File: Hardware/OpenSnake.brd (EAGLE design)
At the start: 25.4 x 25.4 mm, 36 parts, among them J1 microB, Q1 16MHZ, U1 ATMEGA328P_TQFP, U3 CH340G, U4 5V, Y2 12MHz

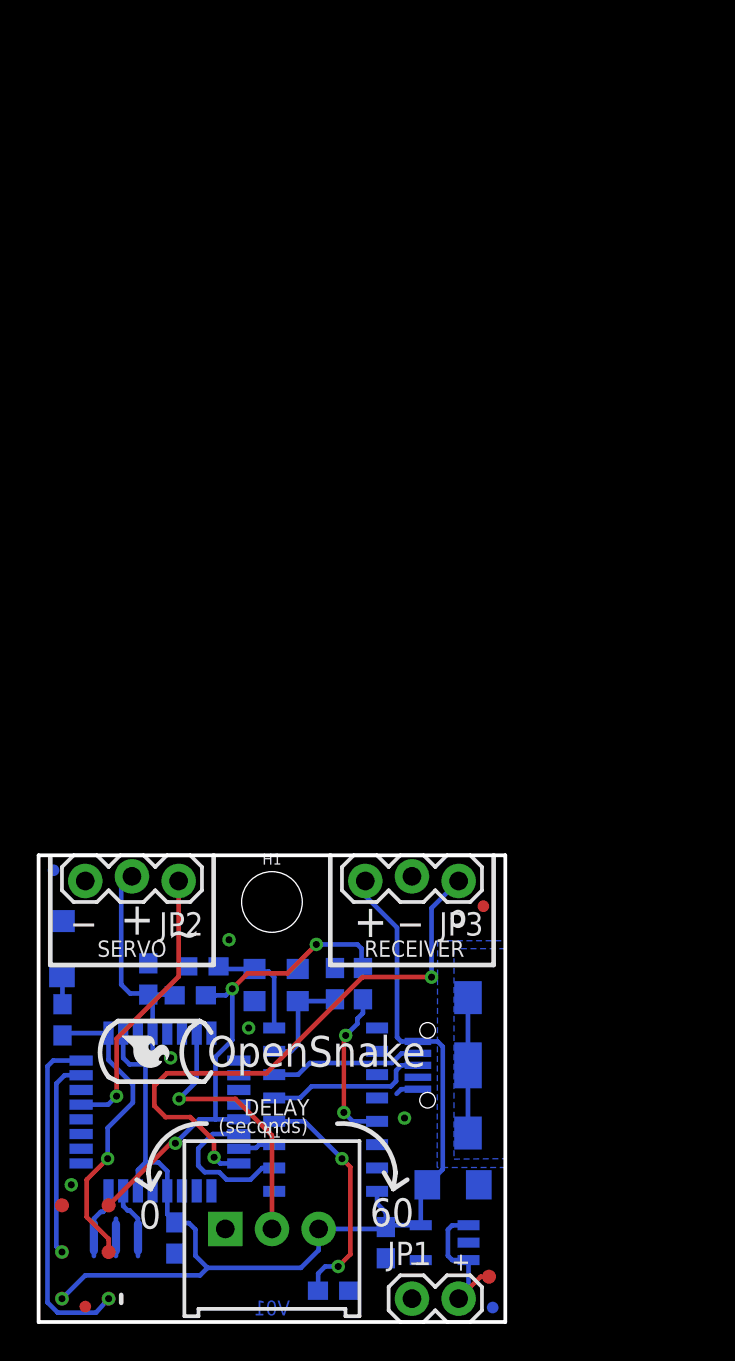
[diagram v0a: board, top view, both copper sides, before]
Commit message: initial idea on pcb layout
the plan is to use some double sided tape and stick this to the side of the can. The 9V battery would also be stuck to the other side.
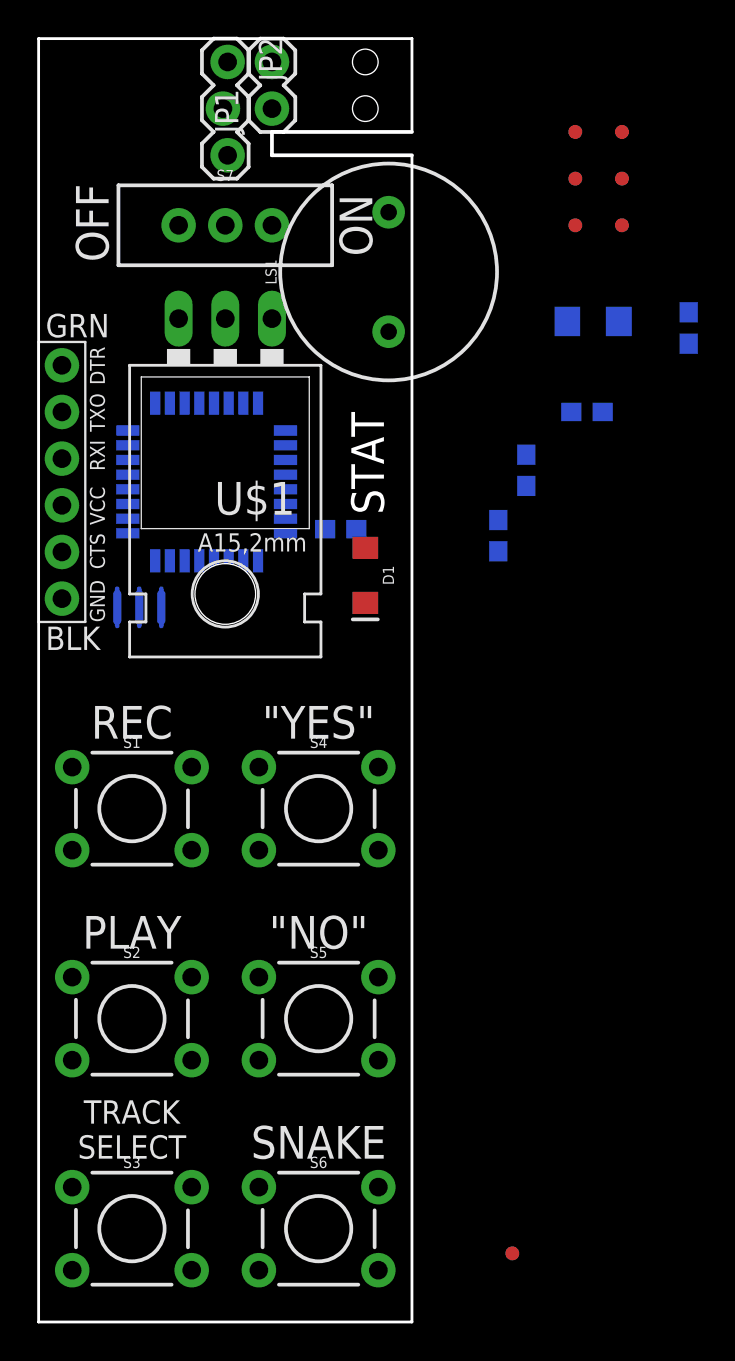
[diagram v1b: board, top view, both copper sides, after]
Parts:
- removed C5, C6: 10pF, SparkFun-Capacitors:0603-CAP
- removed C7: 10nF, SparkFun-Capacitors:0603-CAP
- removed C8: 0.1uF, SparkFun-Capacitors:0603-CAP
- removed FID1, FID2, FID3, FID4: FIDUCIALUFIDUCIAL, SparkFun-Aesthetics:MICRO-FIDUCIAL
- removed H1: STAND-OFF, SparkFun-Hardware:STAND-OFF
- removed JP3: IR Receiver, Testing:1X03_LOCK
- removed LOGO1: SFE_LOGO_FLAME.1_INCH, SparkFun-Aesthetics:SFE_LOGO_FLAME_.1
- removed LOGO2: OSHW-LOGOMINI, SparkFun-Aesthetics:OSHW-LOGO-MINI
- removed R1: TRIMPOT, Jim-Resistors-to-Move:TRIMPOT-PTH-3386U
- removed TP1: TEST-POINT3, SparkFun-Passives:PAD.03X.03
- removed U3: CH340G, SparkFun-DigitalIC:SO016
- removed U4: 5V, SparkFun-IC-Power:SOT23-5
- removed Y2: 12MHz, USB Basic:CRYSTAL-SMD-3.2X2.5
- added LS1: BUZZER-PTH, SparkFun-Electromechanical:BUZZER-12MM
- added S1, S2, S3, S4, S5, S6: (no value), SparkFun-Switches:TACTILE_SWITCH_PTH_6.0MM
- added S7: (no value), SparkFun-Switches:SWITCH_SPDT_PTH_11.6X4.0MM
- added TP8: TEST-POINT3, SparkFun-Passives:PAD.03X.03
- added U$1: V_REG_LD1117VXX, SparkFun-IC-Power:78XXL
- J1: value microB -> (none); device SparkFun-Connectors:USB-B-MICRO-SMD_V03 -> SparkFun-Connectors:6_PIN_SERIAL_TARGET_SIDE_W_SILK
- moved JP1 65.2 mm to (12.7, 66.0), turned to 90 degrees
- moved TP2 64.8 mm to (31.8, 59.7)
- moved TP3 64.8 mm to (29.2, 62.2)
- moved TP4 64.8 mm to (31.8, 62.2)
- moved TP5 64.8 mm to (31.8, 64.8)
- moved TP7 64.8 mm to (29.2, 64.8)
- moved C4 56.9 mm to (35.4, 54.1)
- moved C9 47.6 mm to (30.2, 54.5)
- moved JP2 44.5 mm to (10.2, 68.6), turned to 270 degrees
- moved J1 38.7 mm to (1.27, 45.7), flipped to the top, turned to 270 degrees
- moved R2 38.4 mm to (29.8, 49.5)
- moved U1 34.4 mm to (9.14, 45.7)
- moved Q1 34.3 mm to (5.48, 38.9)
- moved C3 30.7 mm to (25.0, 42.8)
- moved R6 30.7 mm to (16.4, 43.2), turned to 180 degrees
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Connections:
- removed net N$3: C6.2, U3.8, Y2.3
- removed net N$4: C5.2, U3.7, Y2.1
- removed net N$5: J1.D+, U3.5
- removed net N$6: J1.D-, U3.6
- removed net SHLD: J1.SHIELD1, J1.SHIELD2, J1.SHIELD3
- removed net V3: C7.1, U3.4
- net !DTR: no longer U3.13
- net A0: no longer R1.2
- net BATT: no longer U4.1, U4.3
- net D2: no longer JP3.1
- net GND: no longer C5.1, C6.1, C7.2, C8.2, J1.GND, JP3.2, R1.1, U3.1, U3.9, U4.2, Y2.2, Y2.4
- net RX: no longer U3.2
- net TX: no longer U3.3
- net VCC: now also TP8.P$1; no longer C8.1, J1.VBUS, JP3.3, R1.3, TP1.P$1, U3.16, U4.5
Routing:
- net VCC: track 77.3 -> 0.00 mm, vias 1 -> 0
- net D2: track 30.9 -> 0.00 mm, vias 2 -> 0
- net RST: track 27.8 -> 0.00 mm, vias 3 -> 0
- net MISO: track 18.7 -> 0.00 mm, vias 1 -> 0
- net SCK: track 16.6 -> 0.00 mm, vias 1 -> 0
- net D9: track 15.2 -> 0.00 mm, vias 1 -> 0
- net A0: track 14.9 -> 0.00 mm, vias 1 -> 0
- net V3: track 13.1 -> 0.00 mm, vias 2 -> 0
- net MOSI: track 10.8 -> 0.00 mm, vias 1 -> 0
- net N$5: track 8.90 -> 0.00 mm
- net !DTR: track 8.60 -> 0.00 mm, vias 2 -> 0
- net BATT: track 8.33 -> 0.00 mm
- net N$6: track 8.30 -> 0.00 mm
- net RX: track 8.18 -> 0.00 mm
- net SHLD: track 7.37 -> 0.00 mm
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- removed copper zone on layer 1, net GND
- removed copper zone on layer 16, net GND
- removed copper zone on layer 16, net SHLD
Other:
- board size 25.4 x 25.4 mm -> 20.3 x 69.8 mm
- board text added: ""NO""
- board text added: ""YES""
- board text added: "9V Battery"
- board text added: "HINGE"
- board text added: "OFF"
- board text added: "ON"
- board text added: "PLAY"
- board text added: "REC"
- board text added: "SNAKE"
- board text added: "TRACK SELECT"
- board text added: "cable to 9V battery"
- board text added: "cable to servo"
- board text added: "servo"
- board text removed: "(seconds)"
- board text removed: "+"
- board text removed: "-"
- board text removed: "0"
- board text removed: "60"
- board text removed: "DELAY"
- board text removed: "OpenSnake"
- board text removed: "RECEIVER"
- board text removed: "SERVO"
- board text removed: "V01"
- board text removed: "_"
- board text removed: "o"
- board text removed: "~"
